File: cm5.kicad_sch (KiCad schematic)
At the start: 0 parts

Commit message: [#1] WIP: Change components to ones from the global library, refactor schematic
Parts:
- added A1: RPi CM5, DW-footprints:CM5, symbol DW-SoM:CM5
- added H1, H2, H3, H4: Spacer_M2.5_H3mm_9774030151R, DW-footprints:Spacer_M2.5_H3mm_9774030151R, symbol DW-mechanical:Spacer_M2.5_H3mm_9774030151R
- added J7: CM5_101-200_3mm-stack, DW-footprints:Conn_Socket_Hirose_DF40_2x50_DF40HC-3.0-100DS-0.4V, symbol DW-connectors:CM5_101-200_3mm-stack
- added J9: CM5_1-100_3mm-stack, DW-footprints:Conn_Socket_Hirose_DF40_2x50_DF40HC-3.0-100DS-0.4V, symbol DW-connectors:CM5_1-100_3mm-stack
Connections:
- new net: J9.84 (+3.3v_(Output)), J9.86 (+3.3v_(Output))
- new net: J9.88 (+1.8v_(Output)), J9.90 (+1.8v_(Output))
- new net +5v_(Input): J9.77 (+5v_(Input)), J9.79 (+5v_(Input)), J9.81 (+5v_(Input)), J9.83 (+5v_(Input)), J9.85 (+5v_(Input)), J9.87 (+5v_(Input))
- new net ETH.D1+: J9.12 (Ethernet_Pair0_P)
- new net ETH.D1-: J9.10 (Ethernet_Pair0_N)
- new net ETH.D2+: J9.4 (Ethernet_Pair1_P)
- new net ETH.D2-: J9.6 (Ethernet_Pair1_N)
- new net ETH.D3+: J9.11 (Ethernet_Pair2_P)
- new net ETH.D3-: J9.9 (Ethernet_Pair2_N)
- new net ETH.D4+: J9.3 (Ethernet_Pair3_P)
- new net ETH.D4-: J9.5 (Ethernet_Pair3_N)
- new net ETH.LED_ACT: J9.15 (Ethernet_nLED3(3.3v))
- new net ETH.LED_LINK: J9.17 (Ethernet_nLED2(3.3v))
- new net GND: H1.1, H2.1, H3.1, H4.1, J7.13 (GND), J7.14 (GND), J7.19 (GND), J7.20 (GND), J7.25 (GND), J7.26 (GND), J7.31 (GND), J7.32 (GND), J7.37 (GND), J7.38 (GND), J7.44 (GND), J7.50 (GND), J7.55 (GND), J7.56 (GND), J7.61 (GND), J7.62 (GND), J7.67 (GND), J7.68 (GND), J7.7 (GND), J7.73 (GND), J7.74 (GND), J7.79 (GND), J7.8 (GND), J7.80 (GND), J7.85 (GND), J7.86 (GND), J7.91 (GND), J7.92 (GND), J7.97 (GND), J7.98 (GND), J9.1 (GND), J9.13 (GND), J9.14 (GND), J9.2 (GND), J9.22 (GND), J9.23 (GND), J9.32 (GND), J9.33 (GND), J9.42 (GND), J9.43 (GND), J9.52 (GND), J9.53 (GND), J9.59 (GND), J9.60 (GND), J9.65 (GND), J9.66 (GND), J9.7 (GND), J9.71 (GND), J9.74 (GND), J9.8 (GND), J9.98 (GND)
- new net HDMI_0.CEC: J7.51 (HDMI0_CEC)
- new net HDMI_0.CLK+: J7.88 (HDMI0_CLK_P)
- new net HDMI_0.CLK-: J7.90 (HDMI0_CLK_N)
- new net HDMI_0.D0+: J7.82 (HDMI0_TX0_P)
- new net HDMI_0.D0-: J7.84 (HDMI0_TX0_N)
- new net HDMI_0.D1+: J7.76 (HDMI0_TX1_P)
- new net HDMI_0.D1-: J7.78 (HDMI0_TX1_N)
- new net HDMI_0.D2+: J7.70 (HDMI0_TX2_P)
- new net HDMI_0.D2-: J7.72 (HDMI0_TX2_N)
- new net HDMI_0.HOTPLUG: J7.53 (HDMI0_HOTPLUG)
- new net HDMI_0.SCL: J7.100 (HDMI0_SCL)
- new net HDMI_0.SDA: J7.99 (HDMI0_SDA)
- new net HDMI_1.CEC: J7.49 (HDMI1_CEC)
- new net HDMI_1.CLK+: J7.64 (HDMI1_CLK_P)
- new net HDMI_1.CLK-: J7.66 (HDMI1_CLK_N)
- new net HDMI_1.D0+: J7.58 (HDMI1_TX0_P)
- new net HDMI_1.D0-: J7.60 (HDMI1_TX0_N)
- new net HDMI_1.D1+: J7.52 (HDMI1_TX1_P)
- new net HDMI_1.D1-: J7.54 (HDMI1_TX1_N)
- new net HDMI_1.D2+: J7.46 (HDMI1_TX2_P)
- new net HDMI_1.D2-: J7.48 (HDMI1_TX2_N)
- new net HDMI_1.HOTPLUG: J7.43 (HDMI1_HOTPLUG)
- new net HDMI_1.SCL: J7.47 (HDMI1_SCL)
- new net HDMI_1.SDA: J7.45 (HDMI1_SDA)
- new net MIPI_0.CLK+: J7.29 (MIPI0_C_P)
- new net MIPI_0.CLK-: J7.27 (MIPI0_C_N)
- new net MIPI_0.D0+: J7.17 (MIPI0_D0_P)
- new net MIPI_0.D0-: J7.15 (MIPI0_D0_N)
- new net MIPI_0.D1+: J7.23 (MIPI0_D1_P)
- new net MIPI_0.D1-: J7.21 (MIPI0_D1_N)
- new net MIPI_0.D2+: J7.35 (MIPI0_D2_P)
- new net MIPI_0.D2-: J7.33 (MIPI0_D2_N)
- new net MIPI_0.D3+: J7.41 (MIPI0_D3_P)
- new net MIPI_0.D3-: J7.39 (MIPI0_D3_N)
- new net MIPI_1.CLK+: J7.89 (MIPI1_C_P)
- new net MIPI_1.CLK-: J7.87 (MIPI1_C_N)
- new net MIPI_1.D0+: J7.77 (MIPI1_D0_P)
- new net MIPI_1.D0-: J7.75 (MIPI1_D0_N)
- new net MIPI_1.D1+: J7.83 (MIPI1_D1_P)
- new net MIPI_1.D1-: J7.81 (MIPI1_D1_N)
- new net MIPI_1.D2+: J7.95 (MIPI1_D2_P)
- new net MIPI_1.D2-: J7.93 (MIPI1_D2_N)
- new net MIPI_1.D3+: J7.96 (MIPI1_D3_P)
- new net MIPI_1.D3-: J7.94 (MIPI1_D3_N)
- new net PCIe_M2.REFCLK+: J7.10 (PCIe_CLK_P)
- new net PCIe_M2.REFCLK-: J7.12 (PCIe_CLK_N)
- new net PCIe_M2.RX0+: J7.16 (PCIe_RX_P)
- new net PCIe_M2.RX0-: J7.18 (PCIe_RX_N)
- new net PCIe_M2.TX0+: J7.22 (PCIe_TX_P)
- new net PCIe_M2.TX0-: J7.24 (PCIe_TX_N)
- new net SD_CARD.CLK: J9.57 (SD_CLK)
- new net SD_CARD.CMD: J9.62 (SD_CMD)
- new net SD_CARD.DAT0: J9.63 (SD_DAT0)
- new net SD_CARD.DAT1: J9.67 (SD_DAT1)
- new net SD_CARD.DAT2: J9.69 (SD_DAT2)
- new net SD_CARD.DAT3: J9.61 (SD_DAT3)
- new net SD_CARD.DAT4: J9.68 (SD_DAT4)
- new net SD_CARD.DAT5: J9.64 (SD_DAT5)
- new net SD_CARD.DAT6: J9.72 (SD_DAT6)
- new net SD_CARD.DAT7: J9.70 (SD_DAT7)
- new net SD_PWR_ON: J9.75 (SD_PWR_ON)
- new net SD_VDD_Override: J9.73 (SD_VDD_Override)
- new net USB.D+: J7.5 (USB2_P)
- new net USB.D-: J7.3 (USB2_N)
- new net USB_SS_0.D+: J7.34 (USB3-0-D_P)
- new net USB_SS_0.D-: J7.36 (USB3-0-D_N)
- new net USB_SS_0.RX+: J7.30 (USB3-0-RX_P)
- new net USB_SS_0.RX-: J7.28 (USB3-0-RX_N)
- new net USB_SS_0.TX+: J7.42 (USB3-0-TX_P)
- new net USB_SS_0.TX-: J7.40 (USB3-0-TX_N)
- new net USB_SS_1.D+: J7.63 (USB3-1-D_P)
- new net USB_SS_1.D-: J7.65 (USB3-1-D_N)
- new net USB_SS_1.RX+: J7.59 (USB3-1-RX_P)
- new net USB_SS_1.RX-: J7.57 (USB3-1-RX_N)
- new net USB_SS_1.TX+: J7.71 (USB3-1-TX_P)
- new net USB_SS_1.TX-: J7.69 (USB3-1-TX_N)
- new net VBUS_EN: J7.11 (VBUS_EN)
- new net ~{PCIe_M2_CLKREQ}: J7.2 (PCIe_nCLKREQ)
- new net ~{PCIe_M2_PERST}: J7.9 (PCIe_nRST)
- new net ~{PCIe_M2_PWR_EN}: J7.6 (PCIE_PWR_EN)
- new net ~{PCIe_M2_WAKE}: J7.4 (PCIE_nWAKE)
- no-connect marks 0 -> 2

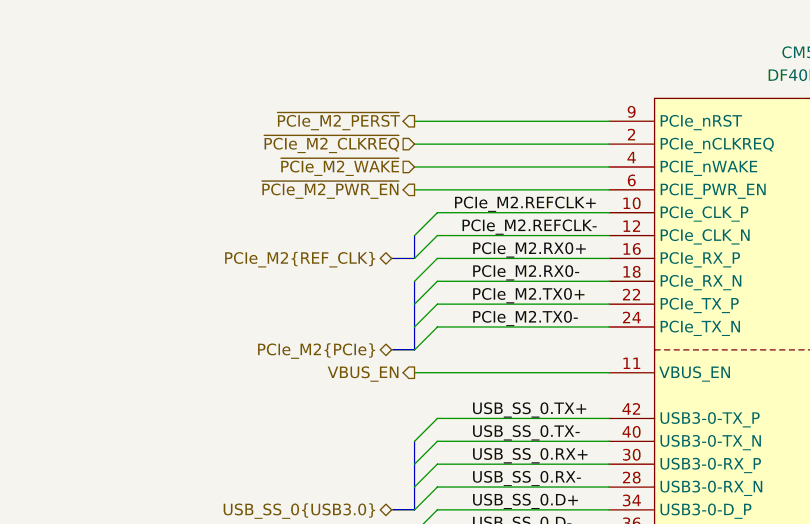
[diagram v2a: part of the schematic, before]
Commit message: [#1] Add bus colors, rename PCIe signals
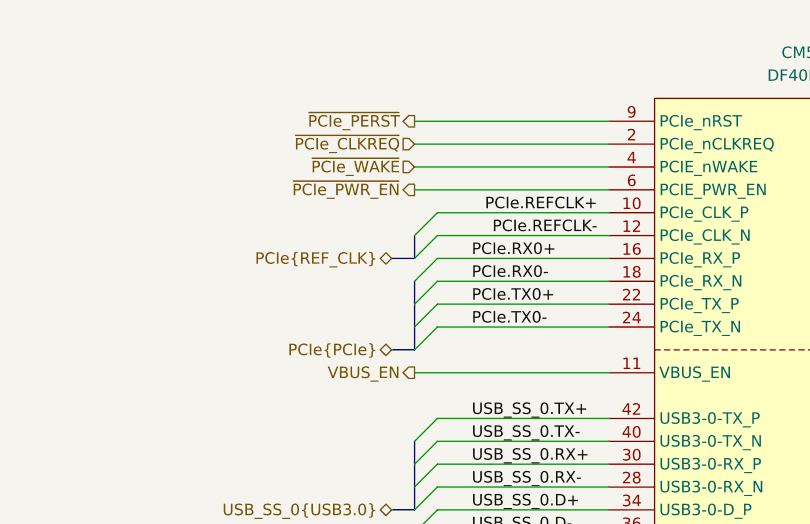
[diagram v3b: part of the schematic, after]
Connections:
- net PCIe_M2.REFCLK+ renamed PCIe.REFCLK+
- net PCIe_M2.REFCLK- renamed PCIe.REFCLK-
- net PCIe_M2.RX0+ renamed PCIe.RX0+
- net PCIe_M2.RX0- renamed PCIe.RX0-
- net PCIe_M2.TX0+ renamed PCIe.TX0+
- net PCIe_M2.TX0- renamed PCIe.TX0-
- net ~{PCIe_M2_CLKREQ} renamed ~{PCIe_CLKREQ}
- net ~{PCIe_M2_PERST} renamed ~{PCIe_PERST}
- net ~{PCIe_M2_PWR_EN} renamed ~{PCIe_PWR_EN}
- net ~{PCIe_M2_WAKE} renamed ~{PCIe_WAKE}

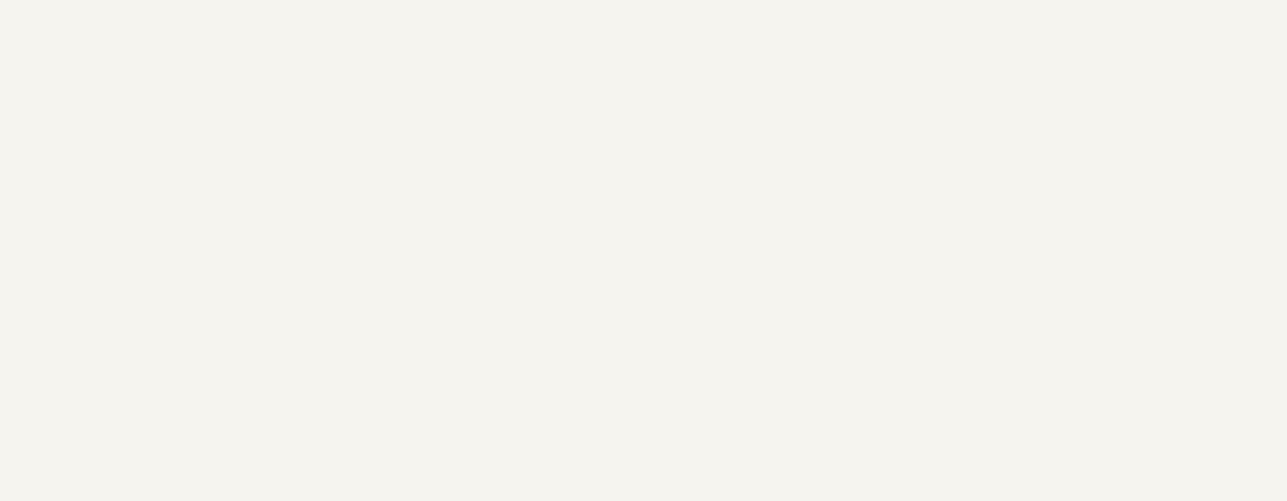
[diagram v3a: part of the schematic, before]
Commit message: [#1] Add debug UART connector
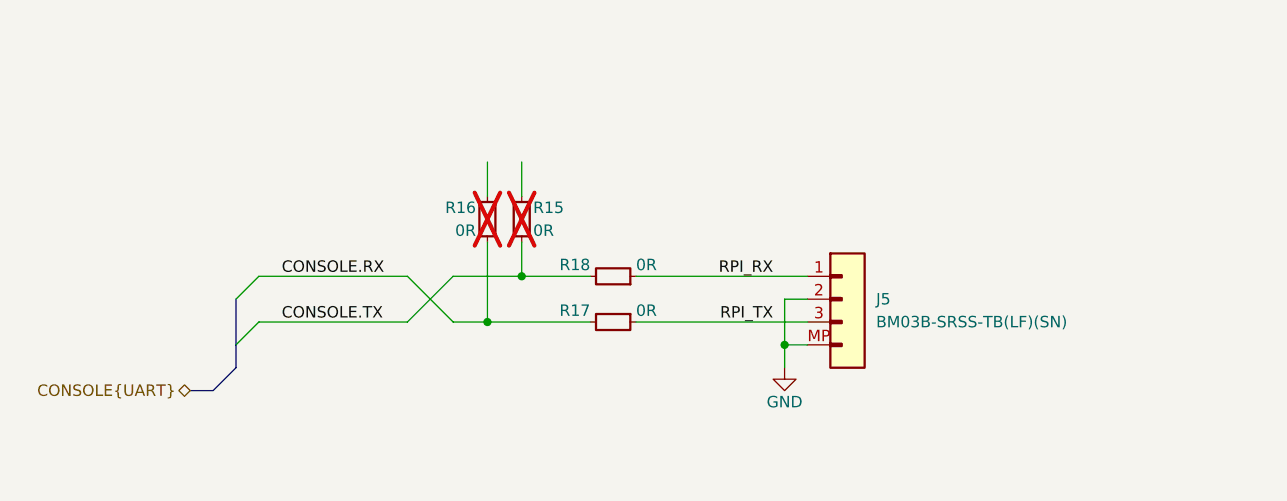
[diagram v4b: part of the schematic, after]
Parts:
- added J5: JST_SH_1x3_BM03B-SRSS-TB-LF-SN, DW-footprints:Conn_JST_SH_1x3_BM03B-SRSS-TB, symbol DW-connectors:JST_SH_1x3_BM03B-SRSS-TB-LF-SN
- added R15, R16, R17, R18: R-0R-0402, DW-footprints:R_0402_1005Metric, symbol DW-resistors:R-0R-0402
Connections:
- net GND: now also J5.2, J5.MP
- new net CONSOLE.RX: R16.1, R17.2
- new net CONSOLE.TX: R15.1, R18.2
- new net RPI_RX: J5.1, R18.1
- new net RPI_TX: J5.3, R17.1

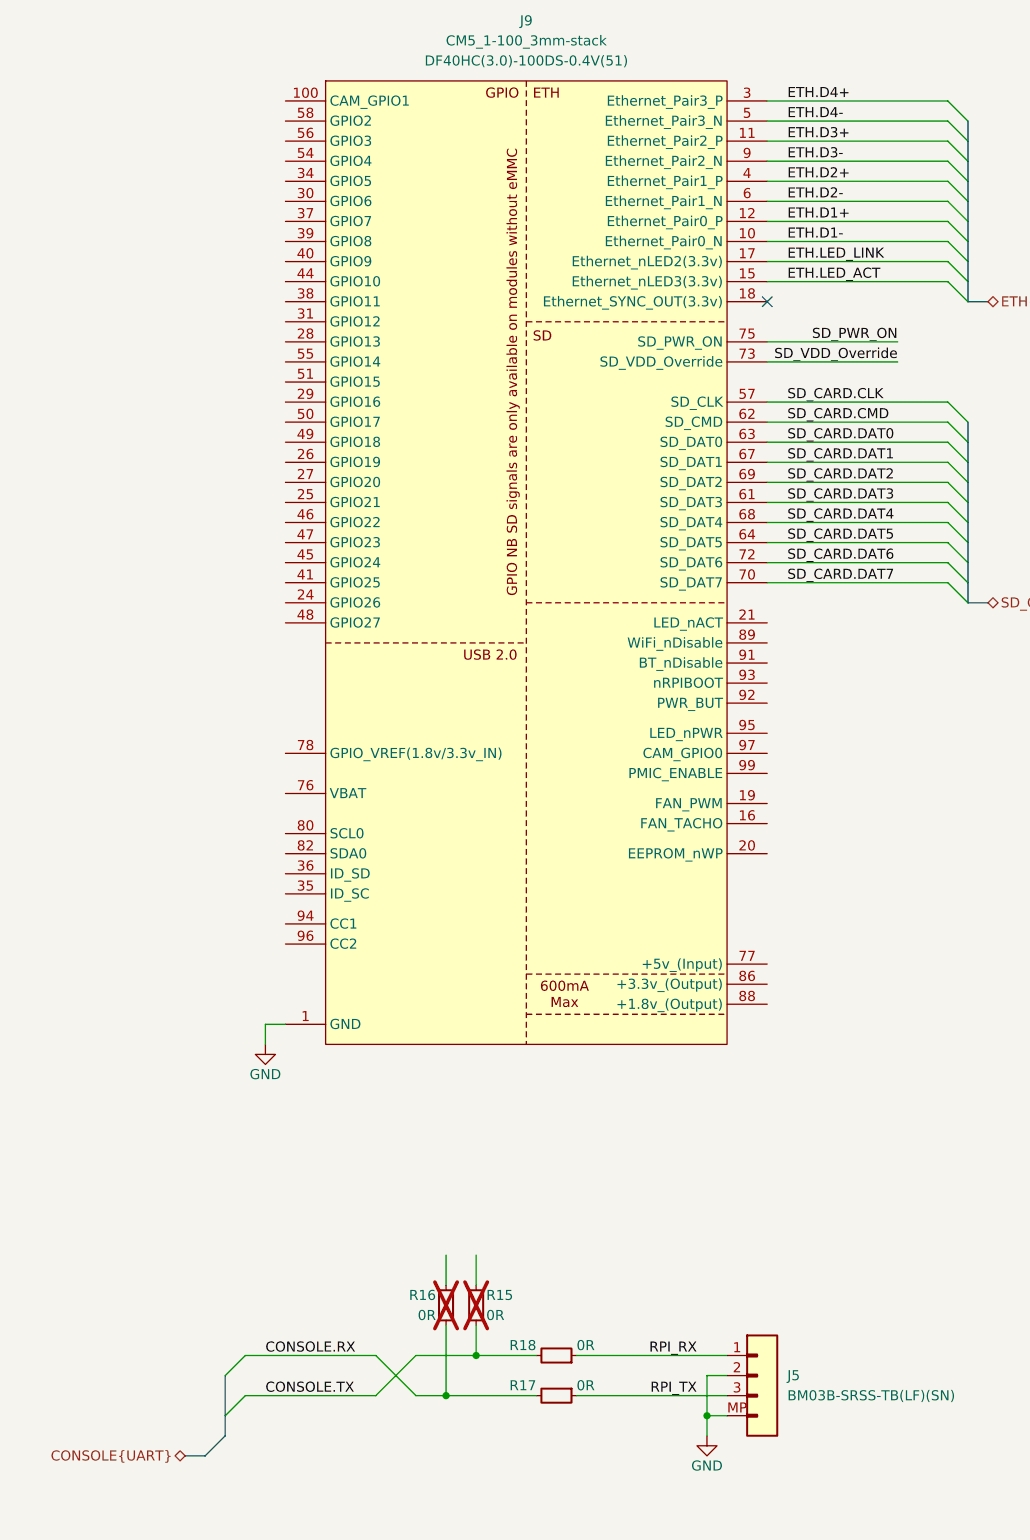
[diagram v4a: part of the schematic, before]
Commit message: [#1] Add level shifter for UART debug, update footprints from library
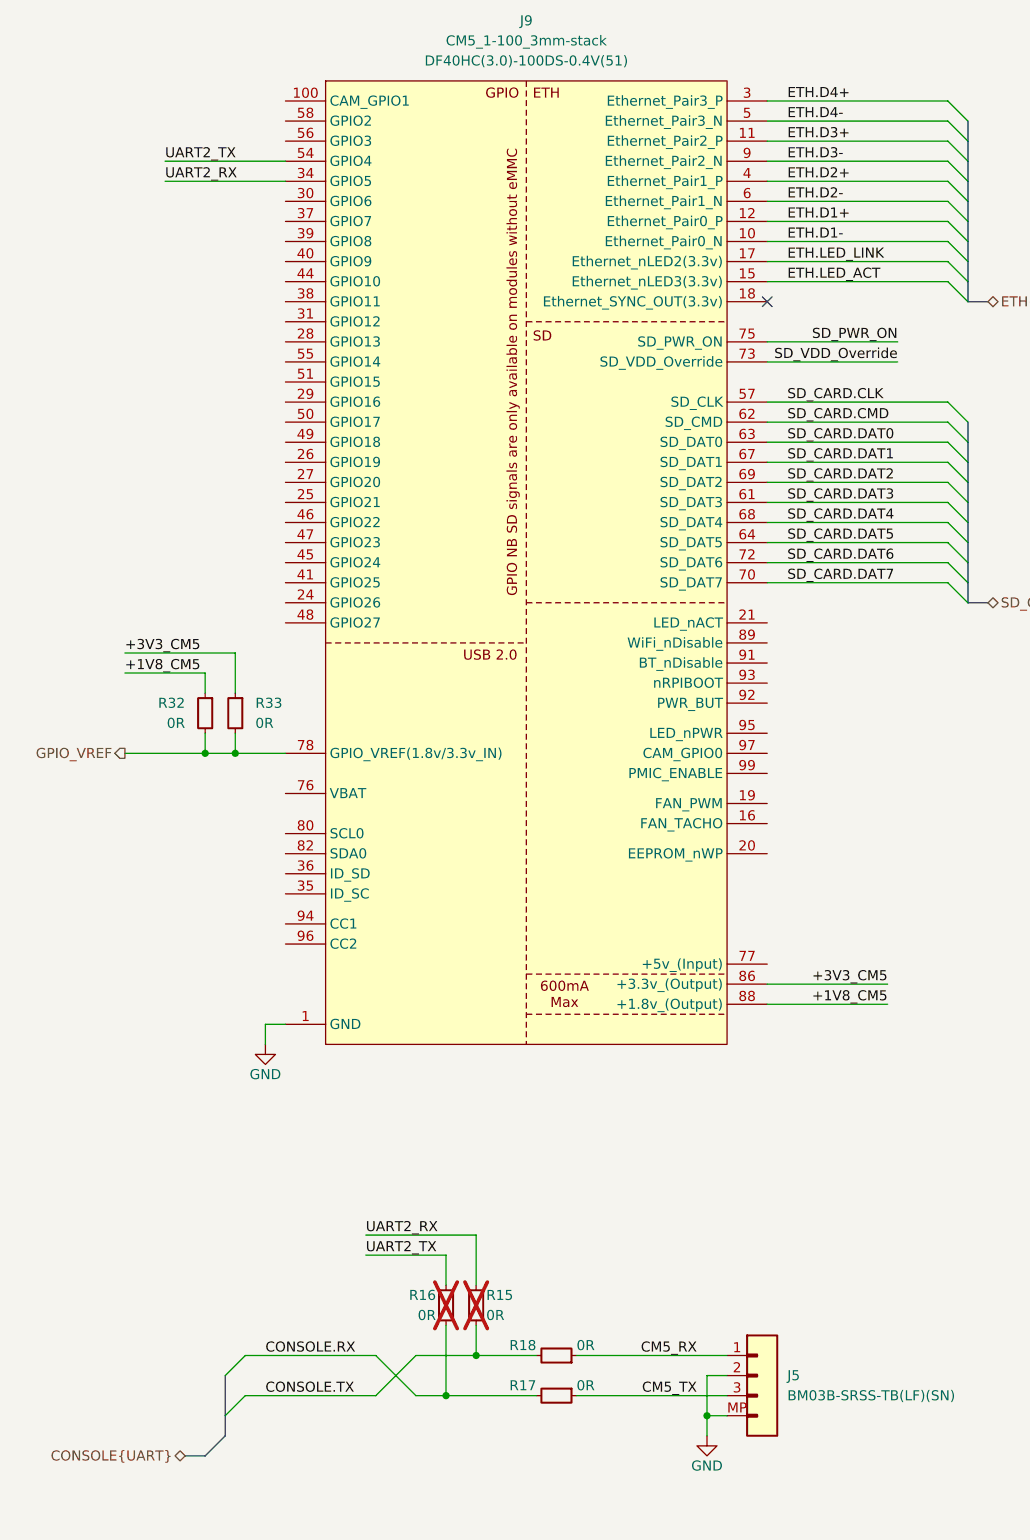
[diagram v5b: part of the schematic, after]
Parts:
- added R32, R33: R-0R-0402, DW-footprints:R_0402_1005Metric, symbol DW-resistors:R-0R-0402
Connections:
- net UART2_RX: now reaches R15.2
- net UART2_RX: now also J9.34 (GPIO5)
- net UART2_TX: now reaches J9.54 (GPIO4)
- net UART2_TX: now also R16.2
- net GPIO_VREF: now reaches J9.78 (GPIO_VREF(1.8v/3.3v_IN))
- net GPIO_VREF: now also R32.2, R33.2
- net +3V3_CM5: now reaches J9.84 (+3.3v_(Output)), J9.86 (+3.3v_(Output))
- net +3V3_CM5: now also R33.1
- net +1V8_CM5: now reaches J9.88 (+1.8v_(Output)), J9.90 (+1.8v_(Output))
- net +1V8_CM5: now also R32.1
- net RPI_RX renamed CM5_RX
- net RPI_TX renamed CM5_TX

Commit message: [#1] Re-annotate schematic
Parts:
- renumbered J9 to J2, J7 to J3, J5 to J4, R32 to R1, R33 to R2, R16 to R3, R15 to R4, R18 to R5, R17 to R6
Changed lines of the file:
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@@
+		(polyline
+			(pts
+				(xy 171.45 85.09) (xy 171.45 115.57) (xy 149.86 115.57) (xy 149.86 85.09)
+			)
+			(stroke
+				(width 0)
+				(type dash)
+			)
+			(fill
+				(type none)
+			)
+		)
+	)
+	(rule_area
 		(polyline
 			(pts
@@
 			(pts
 				(xy 243.84 114.3) (xy 217.17 114.3) (xy 217.17 96.52) (xy 243.84 96.52)
-			)
-			(stroke
-				(width 0)
-				(type dash)
-			)
-			(fill
-				(type none)
-			)
-		)
-	)
-	(rule_area
-		(polyline
-			(pts
-				(xy 171.45 85.09) (xy 171.45 115.57) (xy 149.86 115.57) (xy 149.86 85.09)
 			)
 			(stroke
@@
 		(dnp no)
 		(fields_autoplaced yes)
-		(property "Reference" "R32"
+		(property "Reference" "R1"
 			(at 53.34 163.83 90)
 			(effects
@@
 			(project "cm5-module"
 				(path "/090a8e41-87a8-4fb1-998b-60a2c0dc4cee/dfbce24a-51ce-450d-9d41-776080287e8b"
-					(reference "R32")
+					(reference "R1")
 					(unit 1)
 				)
@@
 		(dnp no)
 		(fields_autoplaced yes)
-		(property "Reference" "J5"
+		(property "Reference" "J4"
 			(at 129.54 248.92 0)
 			(effects
@@
 			(project "cm5-module"
 				(path "/090a8e41-87a8-4fb1-998b-60a2c0dc4cee/dfbce24a-51ce-450d-9d41-776080287e8b"
-					(reference "J5")
+					(reference "J4")
 					(unit 1)
 				)
@@
 		(dnp no)
 		(fields_autoplaced yes)
-		(property "Reference" "J7"
+		(property "Reference" "J3"
 			(at 293.37 77.47 0)
 			(effects
@@
 			(project ""
 				(path "/090a8e41-87a8-4fb1-998b-60a2c0dc4cee/dfbce24a-51ce-450d-9d41-776080287e8b"
-					(reference "J7")
+					(reference "J3")
 					(unit 1)
 				)
@@
 		(on_board yes)
 		(dnp yes)
-		(property "Reference" "R15"
+		(property "Reference" "R4"
 			(at 91.44 238.76 90)
 			(effects
@@
 			(project ""
 				(path "/090a8e41-87a8-4fb1-998b-60a2c0dc4cee/dfbce24a-51ce-450d-9d41-776080287e8b"
-					(reference "R15")
+					(reference "R4")
 					(unit 1)
 				)
@@
 		(on_board yes)
 		(dnp no)
-		(property "Reference" "R18"
+		(property "Reference" "R5"
 			(at 97.79 245.11 0)
 			(effects
@@
 			(project "cm5-module"
 				(path "/090a8e41-87a8-4fb1-998b-60a2c0dc4cee/dfbce24a-51ce-450d-9d41-776080287e8b"
-					(reference "R18")
+					(reference "R5")
 					(unit 1)
 				)
@@
 		(on_board yes)
 		(dnp no)
-		(property "Reference" "R17"
+		(property "Reference" "R6"
 			(at 97.79 250.19 0)
 			(effects
@@
 			(project "cm5-module"
 				(path "/090a8e41-87a8-4fb1-998b-60a2c0dc4cee/dfbce24a-51ce-450d-9d41-776080287e8b"
-					(reference "R17")
+					(reference "R6")
 					(unit 1)
 				)
@@
 		(dnp no)
 		(fields_autoplaced yes)
-		(property "Reference" "J9"
+		(property "Reference" "J2"
 			(at 96.52 77.47 0)
 			(effects
@@
 			(project "cm5-module"
 				(path "/090a8e41-87a8-4fb1-998b-60a2c0dc4cee/dfbce24a-51ce-450d-9d41-776080287e8b"
-					(reference "J9")
+					(reference "J2")
 					(unit 1)
 				)
@@
 		(on_board yes)
 		(dnp no)
-		(property "Reference" "#PWR60"
+		(property "Reference" "#PWR021"
 			(at 242.57 270.51 0)
 			(effects
@@
 			(project "cm5-module"
 				(path "/090a8e41-87a8-4fb1-998b-60a2c0dc4cee/dfbce24a-51ce-450d-9d41-776080287e8b"
-					(reference "#PWR60")
+					(reference "#PWR021")
 					(unit 1)
 				)
@@
 		(dnp no)
 		(fields_autoplaced yes)
-		(property "Reference" "R33"
+		(property "Reference" "R2"
 			(at 62.23 163.83 90)
 			(effects
@@
 			(project "cm5-module"
 				(path "/090a8e41-87a8-4fb1-998b-60a2c0dc4cee/dfbce24a-51ce-450d-9d41-776080287e8b"
-					(reference "R33")
+					(reference "R2")
 					(unit 1)
 				)
@@
 		(on_board yes)
 		(dnp no)
-		(property "Reference" "#PWR011"
+		(property "Reference" "#PWR018"
 			(at 63.5 213.36 0)
 			(effects
@@
 			(project "cm5-module"
 				(path "/090a8e41-87a8-4fb1-998b-60a2c0dc4cee/dfbce24a-51ce-450d-9d41-776080287e8b"
-					(reference "#PWR011")
+					(reference "#PWR018")
 					(unit 1)
 				)
@@
 		(on_board yes)
 		(dnp no)
-		(property "Reference" "#PWR012"
+		(property "Reference" "#PWR019"
 			(at 260.35 213.36 0)
 			(effects
@@
 			(project "cm5-module"
 				(path "/090a8e41-87a8-4fb1-998b-60a2c0dc4cee/dfbce24a-51ce-450d-9d41-776080287e8b"
-					(reference "#PWR012")
+					(reference "#PWR019")
 					(unit 1)
 				)
@@
 		(on_board yes)
 		(dnp yes)
-		(property "Reference" "R16"
+		(property "Reference" "R3"
 			(at 85.09 238.76 90)
 			(effects
@@
 			(project "cm5-module"
 				(path "/090a8e41-87a8-4fb1-998b-60a2c0dc4cee/dfbce24a-51ce-450d-9d41-776080287e8b"
-					(reference "R16")
+					(reference "R3")
 					(unit 1)
 				)
@@
 		(on_board yes)
 		(dnp no)
-		(property "Reference" "#PWR048"
+		(property "Reference" "#PWR020"
 			(at 119.38 262.89 0)
 			(effects
@@
 			(project "cm5-module"
 				(path "/090a8e41-87a8-4fb1-998b-60a2c0dc4cee/dfbce24a-51ce-450d-9d41-776080287e8b"
-					(reference "#PWR048")
+					(reference "#PWR020")
 					(unit 1)
 				)
